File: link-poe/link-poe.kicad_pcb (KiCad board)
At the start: 4 copper layers, 70 x 22 mm, 41 parts, among them J101 2x05_Horizontal, J102 NE8FAH, J103 JAE_DX07S016JA3, J104 2x05_Horizontal, J105 NE8FAH, J106 WAGO-2065, J107 WAGO-2065, J108 WAGO-2065, J109 WAGO-2065, Q301 BSC010N04LS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

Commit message: Update
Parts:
- moved INFO102 24.6 mm to (152.0, 94.8)
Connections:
- net Earth renamed USB-Shield
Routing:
- net GND: track 7.37 -> 13.5 mm, vias 33 -> 45
- net /USB-: track 39.7 -> 38.6 mm
- net VBUS: track 7.65 -> 8.27 mm
- net /USB+: track 31.2 -> 30.6 mm
- added copper zone on B.Cu, net +5V
- removed copper zone on In2.Cu, net +24V
- removed copper zone on In2.Cu, net +5V
- removed copper zone on In2.Cu, net /+24V-Link
- removed copper zone on B.Cu, net GND

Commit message: Update usb + link-poe
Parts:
- C101, C301, C502, C505: footprint Capacitor_SMD:C_0603_1608Metric -> V2_Capacitor_SMD:C_0603
- C501, C503, C504: footprint Capacitor_SMD:C_1210_3225Metric -> V2_Capacitor_SMD:C_1210
- FID101, FID102, FID103: value Fiducial -> Fiducial_Paste
- ICON102: footprint V2_Artwork:Logo_Tiny -> V2_Artwork:Logo_Small
- INFO102: value ORDER-NUMBER -> Order_Number
- J103: value JAE_DX07S016JA3 -> DX07S016JA3
- J106, J107, J108, J109: value WAGO-2065 -> Conn_01x01
- R101, R102, R301, R302, R501, R502: footprint Resistor_SMD:R_0603_1608Metric -> V2_Resistor_SMD:R_0603
- TVS101: value SMAJ36CA -> SMBJ36CA; footprint Diode_SMD:D_SMA -> V2_Diode_SMD:D_SMB
- moved ICON102 15.8 mm to (172.0, 96.8)
- moved C101 5.94 mm to (150.0, 98.5), turned to 180 degrees
- moved TVS101 0.25 mm to (155.5, 98.5)
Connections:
- net USB-Shield renamed Earth
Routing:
- net GND: vias 45 -> 48

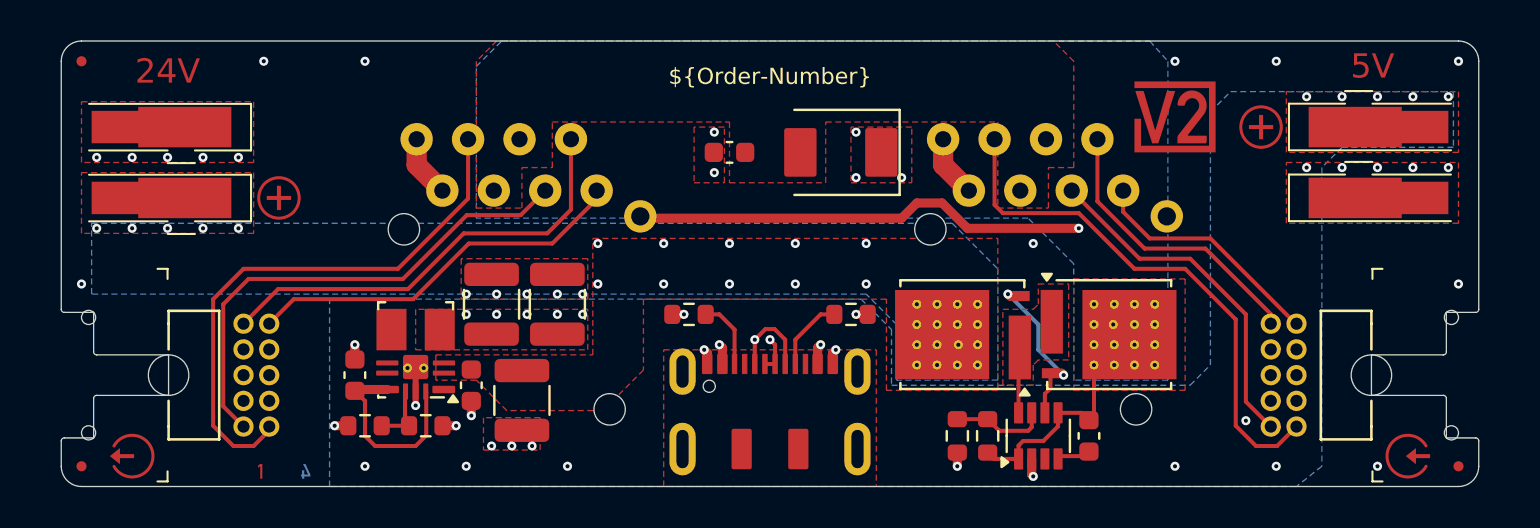
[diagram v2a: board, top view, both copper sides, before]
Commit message: Update power symbols
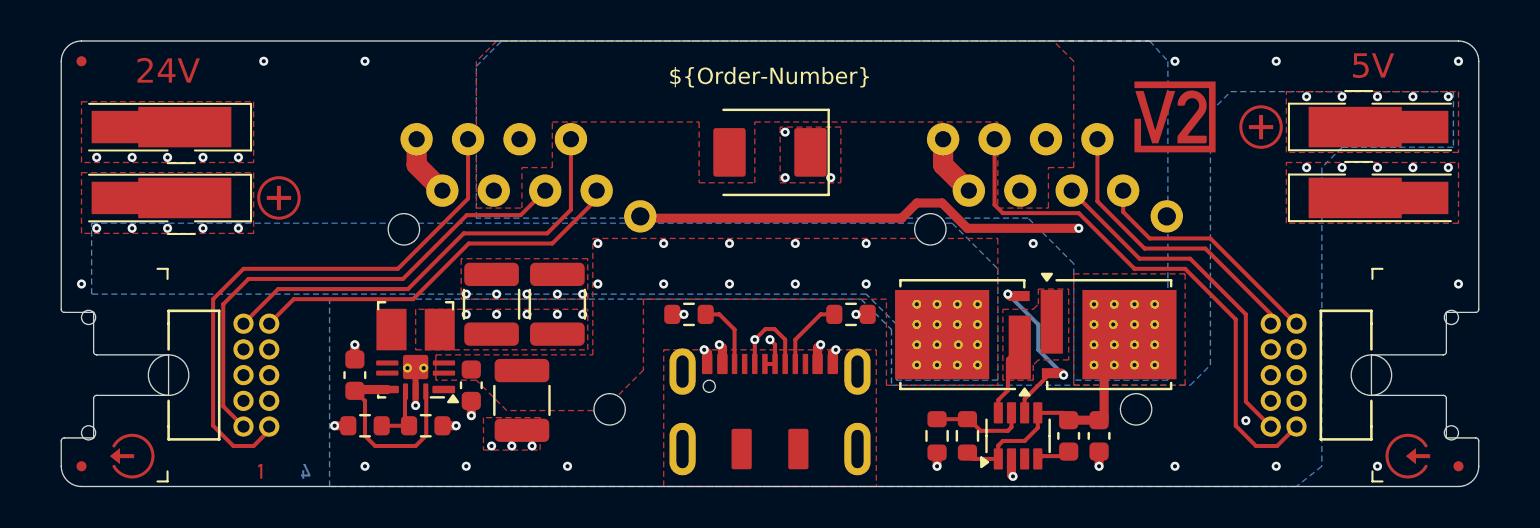
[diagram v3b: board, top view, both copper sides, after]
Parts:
- removed C101: 0u1, V2_Capacitor_SMD:C_0603
- added C301: 0u1, V2_Capacitor_SMD:C_0603, F.Cu at (168.2, 112.5)
- J106, J107, J108, J109: value Conn_01x01 -> WAGO 2065-100
- moved TVS101 3.50 mm to (152.0, 98.5)
- moved C302 1.00 mm to (166.8, 112.5)
- moved R301 1.00 mm to (161.8, 112.5)
- moved R302 1.00 mm to (160.2, 112.5)
- moved U301 1.00 mm to (164.2, 112.5)
- renumbered C301 to C302, ICON106 to ICON105, ICON105 to ICON106
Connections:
- net /Shield renamed /Link-Shield
- net Earth renamed Shield
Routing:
- net /+24V-Link: track 10.1 -> 13.4 mm
- net GND: track 13.5 -> 14.2 mm, vias 48 -> 47

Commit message: Update parts
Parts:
- moved TVS101 1.25 mm to (152.0, 97.2), turned to 90 degrees
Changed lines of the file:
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@@
 	(footprint "V2_Diode_SMD:D_SMB"
 		(layer "F.Cu")
-		(at 152 98.5 180)
+		(at 152 97.25 90)
 		(descr "Diode SMB (DO-214AA)")
 		(tags "Diode SMB (DO-214AA)")
 		(property "Reference" "TVS101"
-			(at 0 -3 180)
+			(at 0 -3 90)
 			(layer "F.SilkS")
 			(hide yes)
@@
 		)
 		(property "Value" "SMBJ36CA"
-			(at 0 3.1 180)
+			(at 0 3.1 90)
 			(layer "F.Fab")
 			(hide yes)
@@
 		)
 		(property "Datasheet" ""
-			(at 0 0 180)
+			(at 0 0 90)
 			(unlocked yes)
 			(layer "F.Fab")
@@
 		)
 		(property "Description" ""
-			(at 0 0 180)
+			(at 0 0 90)
 			(unlocked yes)
 			(layer "F.Fab")
@@
 		(attr smd)
 		(fp_line
-			(start -2.9 2.1)
-			(end 2.3 2.1)
+			(start -2.9 -2.1)
+			(end 2.3 -2.1)
 			(stroke
 				(width 0.12)
@@
 		(fp_line
 			(start -2.9 -2.1)
-			(end 2.3 -2.1)
+			(end -2.9 2.1)
 			(stroke
 				(width 0.12)
@@
 		)
 		(fp_line
-			(start -2.9 -2.1)
-			(end -2.9 2.1)
+			(start -2.9 2.1)
+			(end 2.3 2.1)
 			(stroke
 				(width 0.12)
@@
 		)
 		(fp_line
-			(start 2.3 2)
-			(end -2.3 2)
+			(start 2.3 -2)
+			(end -2.3 -2)
 			(stroke
 				(width 0.1)
@@
 		)
 		(fp_line
-			(start 2.3 -2)
-			(end -2.3 -2)
+			(start 2.3 2)
+			(end -2.3 2)
 			(stroke
 				(width 0.1)
@@
 		)
 		(fp_text user "${REFERENCE}"
-			(at 0 0 180)
+			(at 0 0 90)
 			(layer "F.Fab")
 			(effects
@@
 		)
 		(pad "1" smd roundrect
-			(at -2 0 180)
+			(at -2 0 90)
 			(size 1.6 2.4)
 			(layers "F.Cu" "F.Mask" "F.Paste")
@@
 		)
 		(pad "2" smd roundrect
-			(at 2 0 180)
+			(at 2 0 90)
 			(size 1.6 2.4)
 			(layers "F.Cu" "F.Mask" "F.Paste")
@@
 	)
 	(via
-		(at 155 99.75)
+		(at 153.25 98)
 		(size 0.45)
 		(drill 0.2)
@@
 	)
 	(via
-		(at 152.75 97.5)
+		(at 150.75 98)
 		(size 0.45)
 		(drill 0.2)
@@
 	)
 	(via
-		(at 152.75 99.75)
+		(at 152 98)
 		(size 0.45)
 		(drill 0.2)
@@
 		(polygon
 			(pts
-				(xy 152.5 100) (xy 155.5 100) (xy 155.5 97.25) (xy 152.5 97.25)
+				(xy 150.5 100.25) (xy 153.5 100.25) (xy 153.5 97.75) (xy 150.5 97.75)
 			)
 		)
@@
 			(pts
 				(xy 138.5 93) (xy 137.5 94) (xy 137.5 101.25) (xy 139.75 101.25) (xy 139.75 99.25) (xy 141.25 99.25)
-				(xy 141.25 97) (xy 148.5 97) (xy 148.5 100) (xy 151.25 100) (xy 151.25 97) (xy 163.25 97) (xy 163.25 101.25)
-				(xy 165.75 101.25) (xy 165.75 99.25) (xy 167 99.25) (xy 167 94) (xy 166 93)
+				(xy 141.25 97) (xy 163.25 97) (xy 163.25 101.25) (xy 165.75 101.25) (xy 165.75 99.25) (xy 167 99.25)
+				(xy 167 94) (xy 166 93)
 			)
 		)

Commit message: Refresh
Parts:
- moved TVS101 0.75 mm to (152.0, 98.0)
- moved INFO102 0.50 mm to (152.0, 94.2)
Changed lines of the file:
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@@
 	(footprint "V2_Production:Order_Number"
 		(layer "F.Cu")
-		(at 152 94.75)
+		(at 152 94.25)
 		(property "Reference" "INFO102"
 			(at 0 -1.77 0)
@@
 	(footprint "V2_Diode_SMD:D_SMB"
 		(layer "F.Cu")
-		(at 152 97.25 90)
+		(at 152 98 90)
 		(descr "Diode SMB (DO-214AA)")
 		(tags "Diode SMB (DO-214AA)")
@@
 	)
 	(via
-		(at 153.25 98)
+		(at 153.25 98.75)
 		(size 0.45)
 		(drill 0.2)
@@
 	)
 	(via
-		(at 150.75 98)
+		(at 150.75 98.75)
 		(size 0.45)
 		(drill 0.2)
@@
 	)
 	(via
-		(at 152 98)
+		(at 152 98.75)
 		(size 0.45)
 		(drill 0.2)
@@
 		(polygon
 			(pts
-				(xy 150.5 100.25) (xy 153.5 100.25) (xy 153.5 97.75) (xy 150.5 97.75)
+				(xy 150.5 101) (xy 153.5 101) (xy 153.5 98.5) (xy 150.5 98.5)
 			)
 		)

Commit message: Fix WAGOs
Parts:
- moved FID101 1.00 mm to (117.0, 114.0)
- moved FID102 1.00 mm to (117.0, 94.0)
- moved FID103 1.00 mm to (187.0, 114.0)
- moved ICON104 1.00 mm to (121.2, 94.5)
- moved ICON105 1.00 mm to (184.5, 113.5)
- moved ICON107 1.00 mm to (119.5, 113.5)
- moved J101 1.00 mm to (179.0, 109.5)
- moved J104 1.00 mm to (125.0, 109.5)
- moved J106 1.00 mm to (121.5, 100.8)
- moved J107 1.00 mm to (182.5, 97.2)
- moved J108 1.00 mm to (182.5, 100.8)
- moved J109 1.00 mm to (121.5, 97.2)
- moved PLUG101 1.00 mm to (179.0, 109.5)
- moved PLUG102 1.00 mm to (125.0, 109.5)
- moved ICON103 0.50 mm to (176.8, 97.2)
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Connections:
- net /+24V-Link renamed +VLINK
- net VBUS renamed +VBUS
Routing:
- net /USB-: track 38.6 -> 40.4 mm
- net /Socket-TX-Y: track 24.7 -> 25.7 mm
- net /USB+: track 30.6 -> 31.6 mm
- net /Socket-TX-Z: track 27.5 -> 28.5 mm
- net /Socket-RX-B: track 22.0 -> 23.0 mm
- net /Plug-TX-Z: track 14.4 -> 15.4 mm
- net /Plug-TX-Y: track 11.9 -> 12.9 mm
- net /Plug-RX-A: track 17.2 -> 18.2 mm
- net /Plug-RX-B: track 26.6 -> 27.6 mm
- net /Socket-RX-A: track 19.7 -> 20.7 mm
- net GND: vias 47 -> 51
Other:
- board size 70 x 22 mm -> 72 x 22 mm

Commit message: Use date as revision
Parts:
- ICON104: value 24V -> 28V; footprint V2_Artwork:24V -> V2_Artwork:28V
- TVS101: value SMBJ36CA -> SMBJ33CA
- U501: value TPSM33625 -> TPSM33625RDNR; footprint V2_Converter_DCDC:TPSM33625 -> V2_Converter_DCDC:QFN-11
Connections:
- net +24V renamed +28V
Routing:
- net GND: vias 51 -> 50

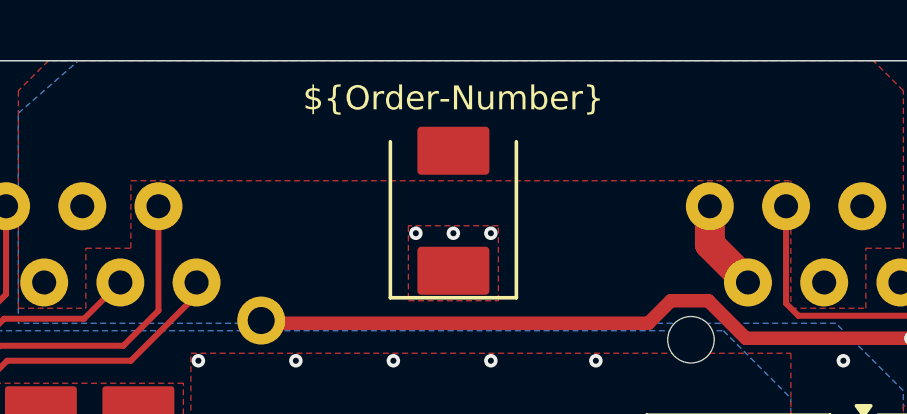
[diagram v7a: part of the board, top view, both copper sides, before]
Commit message: Replace Order_Number
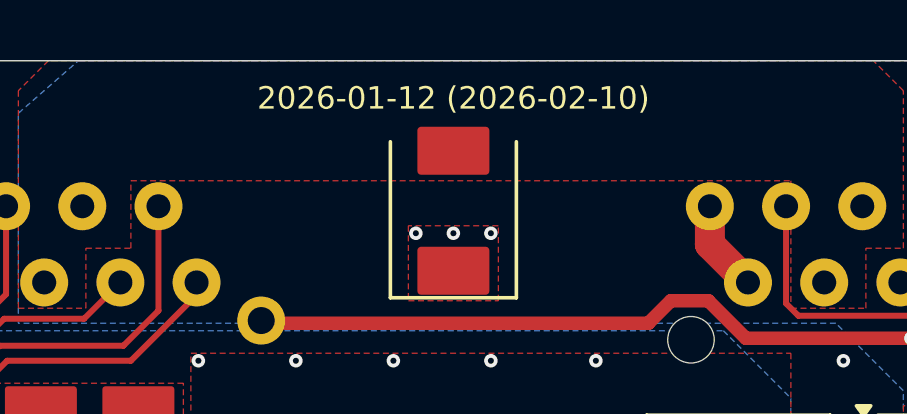
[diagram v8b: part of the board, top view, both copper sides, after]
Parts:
- ICON104: value 28V -> ~
- INFO102: value Order_Number -> ~; footprint V2_Production:Order_Number -> V2_Production:Revision
- U501: value TPSM33625RDNR -> TPSM33625
